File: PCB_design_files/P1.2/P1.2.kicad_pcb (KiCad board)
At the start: 2 copper layers, 127 x 127 mm, 37 parts, among them J1 -EEG_INPUT, J2 +EEG_INPUT, J3 +3.3V, J4 GND, J5 -3V3, J6 EEG_INPUT, J7 STAGE_1_OUT, J8 STAGE_2_OUT, J9 STAGE_3_OUT, U1 INA819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

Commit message: fixed some IC symbols
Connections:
- C6 pad 1: -3V3 -> GND
- C6 pad 2: GND -> -3V3
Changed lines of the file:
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@@
       (stroke (width 0.1) (type solid)) (fill none) (layer "F.Fab"))
     (pad "1" thru_hole rect (at 0 0) (size 1.6 1.6) (drill 0.8) (layers "*.Cu" "*.Mask")
+      (net 1 "GND") (pintype "passive"))
+    (pad "2" thru_hole circle (at 2.5 0) (size 1.6 1.6) (drill 0.8) (layers "*.Cu" "*.Mask")
       (net 8 "-3V3") (pintype "passive"))
-    (pad "2" thru_hole circle (at 2.5 0) (size 1.6 1.6) (drill 0.8) (layers "*.Cu" "*.Mask")
-      (net 1 "GND") (pintype "passive"))
     (model "${KICAD6_3DMODEL_DIR}/Capacitor_THT.3dshapes/CP_Radial_D5.0mm_P2.50mm.wrl"
       (offset (xyz 0 0 0))

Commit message: Created PCB Layout
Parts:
- added J10: BAT+, TestPoint:TestPoint_Loop_D2.50mm_Drill1.0mm, F.Cu at (107.2, 137.6)
- added J11: BOOST, TestPoint:TestPoint_Loop_D2.50mm_Drill1.0mm, F.Cu at (153.9, 106.9)
- J1: value -EEG_INPUT -> EEG_IN-
- J2: value +EEG_INPUT -> EEG_IN+
- R13: value 50k -> 100k
- U4: value TC1044 -> TC1044S
- moved U3 91.5 mm to (146.6, 68.7), turned to 0 degrees
- moved J9 88.2 mm to (181.1, 81.5)
- moved R9 87.4 mm to (154.7, 56.1)
- moved R11 76.8 mm to (168.1, 76.5), turned to 180 degrees
- moved R4 73.7 mm to (130.0, 99.5)
- moved J5 72.7 mm to (142.7, 137.6)
- moved R8 69.6 mm to (150.1, 91.4)
- moved C4 68.0 mm to (146.6, 61.2)
- moved R10 66.0 mm to (154.7, 61.2)
- moved C8 64.8 mm to (158.1, 71.4)
- moved J2 60.8 mm to (81.8, 86.6)
- moved L1 60.7 mm to (119.9, 109.7), turned to -90 degrees
- moved J3 57.7 mm to (119.9, 137.6)
- moved R2 57.6 mm to (98.0, 68.8)
- moved R7 57.4 mm to (130.6, 81.5)
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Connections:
- net Net-(BT1-+) renamed BAT+
- net Net-(J1-Pin_1) renamed /EEG_IN-
- net Net-(J2-Pin_1) renamed /EEG_IN+
- net Net-(J7-Pin_1) renamed STAGE_1_OUT
- C4 pad 1: Net-(J8-Pin_1) -> STAGE_2_OUT
- J8 pad 1: Net-(J8-Pin_1) -> STAGE_2_OUT
- R13 pad 1: Conditioned_EEG -> STAGE_2_OUT
- R13 pad 2: Net-(U3-IN2-) -> Net-(U3-IN1-)
- R8 pad 1: +3.3V -> Net-(U3-IN2-)
- R8 pad 2: Net-(U3-IN1-) -> Conditioned_EEG
- U3 pad 1: Net-(J8-Pin_1) -> STAGE_2_OUT
- U4 pad 1: GND -> Net-(J11-Pin_1)
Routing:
- net +3.3V: track 0.00 -> 172.1 mm
- net -3V3: track 0.00 -> 152.3 mm
- net BAT+: track 0.00 -> 105.3 mm
- net Conditioned_EEG: track 0.00 -> 54.3 mm
- net /EEG_IN-: track 0.00 -> 43.8 mm
- net GND: track 0.00 -> 40.6 mm, vias 0 -> 1
- net /EEG_IN+: track 0.00 -> 39.4 mm
- net Net-(U3-IN1-): track 0.00 -> 34.4 mm
- net Net-(U3-IN2-): track 0.00 -> 34.4 mm
- net STAGE_1_OUT: track 0.00 -> 25.8 mm
- net STAGE_2_OUT: track 0.00 -> 22.7 mm
- net Net-(R2-Pad2): track 0.00 -> 20.8 mm
- net Net-(C8-Pad2): track 0.00 -> 18.1 mm
- net Net-(U4-CAP+): track 0.00 -> 15.7 mm
- net Net-(R2-Pad1): track 0.00 -> 15.0 mm
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- added copper zone on F.Cu, net +3.3V
- added copper zone on B.Cu, net GND
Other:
- board size 127 x 127 mm -> 111.8 x 91.7 mm

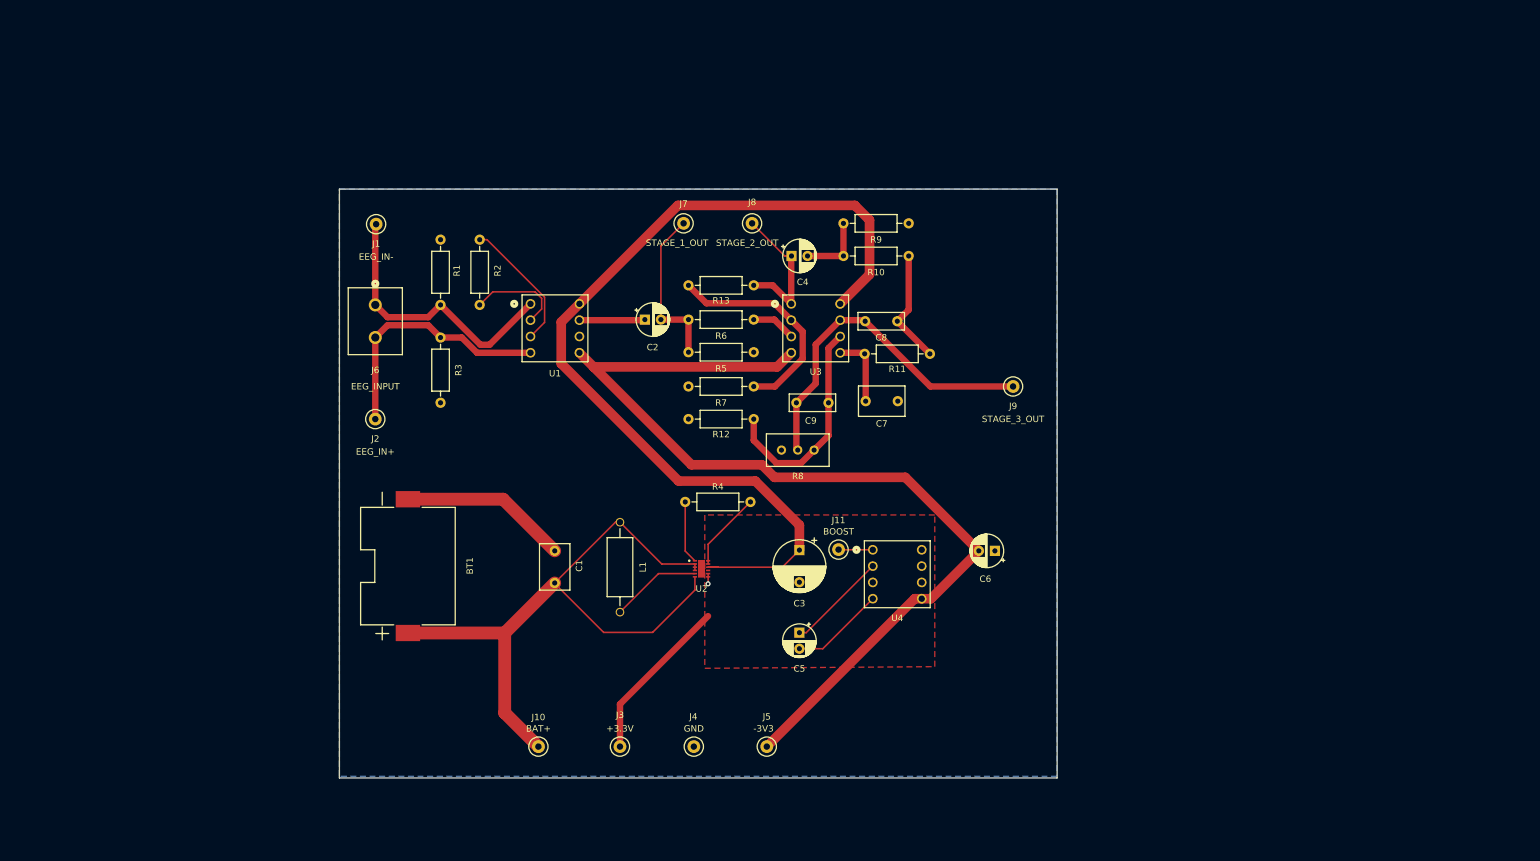
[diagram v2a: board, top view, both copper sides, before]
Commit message: Updated resistor values
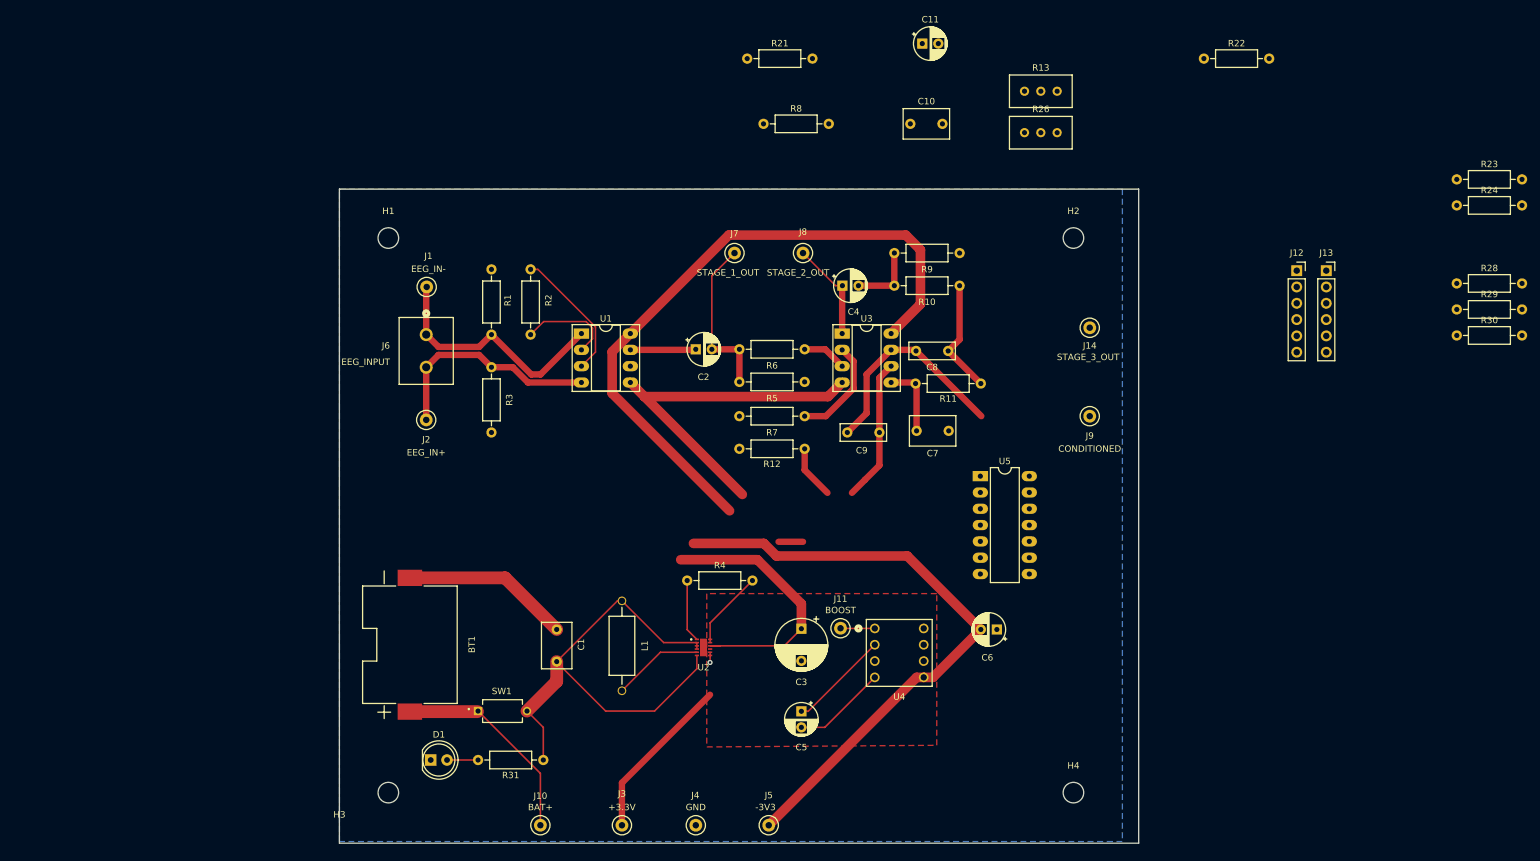
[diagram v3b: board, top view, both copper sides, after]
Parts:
- added C10: 0.1uF, Capacitor_THT:C_Rect_L7.0mm_W4.5mm_P5.00mm, F.Cu at (165.1, 40.6)
- added C11: 10uF, Capacitor_THT:CP_Radial_D5.0mm_P2.50mm, F.Cu at (167.0, 28.1)
- added D1: LED_PWR, LED_THT:LED_D5.0mm, F.Cu at (90.4, 139.7)
- added H1: MountingHole, MountingHole:MountingHole_3.2mm_M3, F.Cu at (83.8, 58.4)
- added H2: MountingHole, MountingHole:MountingHole_3.2mm_M3, F.Cu at (190.5, 58.4)
- added H3: MountingHole, MountingHole:MountingHole_3.2mm_M3, F.Cu at (83.8, 144.8)
- added H4: MountingHole, MountingHole:MountingHole_3.2mm_M3, F.Cu at (190.5, 144.8)
- added J12: Conn_01x06_Pin, Connector_PinSocket_2.54mm:PinSocket_1x06_P2.54mm_Vertical, F.Cu at (225.3, 63.5)
- added J13: Conn_01x06_Pin, Connector_PinSocket_2.54mm:PinSocket_1x06_P2.54mm_Vertical, F.Cu at (229.9, 63.5)
- added J14: STAGE_3_OUT, TestPoint:TestPoint_Loop_D2.50mm_Drill1.0mm, F.Cu at (193.0, 72.4)
- added R21: 100k, Resistor_THT:R_Axial_DIN0207_L6.3mm_D2.5mm_P10.16mm_Horizontal, F.Cu at (139.7, 30.5)
- added R22: 100k, Resistor_THT:R_Axial_DIN0207_L6.3mm_D2.5mm_P10.16mm_Horizontal, F.Cu at (210.8, 30.5)
- added R23: 49.9k, Resistor_THT:R_Axial_DIN0207_L6.3mm_D2.5mm_P10.16mm_Horizontal, F.Cu at (250.2, 49.3)
- added R24: 200k, Resistor_THT:R_Axial_DIN0207_L6.3mm_D2.5mm_P10.16mm_Horizontal, F.Cu at (250.2, 53.3)
- added R26: 100k, Potentiometer_THT:Potentiometer_Bourns_3296W_Vertical, F.Cu at (188.0, 42.0)
- added R28: 10k, Resistor_THT:R_Axial_DIN0207_L6.3mm_D2.5mm_P10.16mm_Horizontal, F.Cu at (250.2, 65.5)
- added R29: 6.98k, Resistor_THT:R_Axial_DIN0207_L6.3mm_D2.5mm_P10.16mm_Horizontal, F.Cu at (250.2, 69.5)
- added R30: 49.9k, Resistor_THT:R_Axial_DIN0207_L6.3mm_D2.5mm_P10.16mm_Horizontal, F.Cu at (250.2, 73.6)
- added R31: 10k, Resistor_THT:R_Axial_DIN0207_L6.3mm_D2.5mm_P10.16mm_Horizontal, F.Cu at (108.0, 139.7)
- added SW1: DS04-254-1S-01BK, DS04_254_1S_01BK:SW_DS04-254-1S-01BK, F.Cu at (101.6, 132.1)
- added U5: LTC1059CS#PBF, Package_DIP:DIP-14_W7.62mm_LongPads, F.Cu at (176.0, 95.5)
- J9: value STAGE_3_OUT -> CONDITIONED
- R10: value 600 -> 604
- R12: value 2.5k -> 2.49k
- R13: footprint Resistor_THT:R_Axial_DIN0207_L6.3mm_D2.5mm_P10.16mm_Horizontal -> Potentiometer_THT:Potentiometer_Bourns_3296W_Vertical
- R2: value 8.5k -> 8.2k
- R8: value 100k -> 49.9k; footprint Potentiometer_THT:Potentiometer_Bourns_3296W_Vertical -> Resistor_THT:R_Axial_DIN0207_L6.3mm_D2.5mm_P10.16mm_Horizontal
- U1, U3: footprint 1-2199298-2:CONN8_1-2199298-2_TEC -> Package_DIP:DIP-8_W7.62mm_Socket_LongPads
- moved R13 56.1 mm to (188.0, 35.6), turned to 0 degrees
- moved R8 51.4 mm to (142.2, 40.6)
- moved J9 12.8 mm to (193.0, 86.2)
- moved J1 12.6 mm to (89.8, 66.0)
- moved J10 12.2 mm to (107.5, 149.9)
- moved J3 12.2 mm to (120.2, 149.9)
- moved J4 12.2 mm to (131.7, 149.9)
- moved J5 12.2 mm to (143.1, 149.9)
- moved BT1 12.2 mm to (87.2, 121.8)
- moved C1 12.2 mm to (110.0, 124.4)
- moved C3 12.2 mm to (148.1, 119.3)
- moved C5 12.2 mm to (148.1, 132.1)
- moved C6 12.2 mm to (178.6, 119.4)
- moved J11 12.2 mm to (154.2, 119.2)
- moved R4 12.2 mm to (130.4, 111.8)
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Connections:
- C1 pad 1: BAT+ -> Net-(U2-EN)
- C8 pad 1: Conditioned_EEG -> Net-(C10-Pad1)
- C9 pad 1: Conditioned_EEG -> Net-(C10-Pad1)
- L1 pad 1: BAT+ -> Net-(U2-EN)
- R13 pad 1: STAGE_2_OUT -> Net-(U3-IN1-)
- R13 pad 2: Net-(U3-IN1-) -> STAGE_2_OUT
- R8 pad 2: Conditioned_EEG -> Net-(C10-Pad1)
- U2 pad 2: BAT+ -> Net-(U2-EN)
- U2 pad 3: BAT+ -> Net-(U2-EN)
- U2 pad 4: BAT+ -> Net-(U2-EN)
- U2 pad 6: BAT+ -> Net-(U2-EN)
- U3 pad 7: Conditioned_EEG -> Net-(U3-OUT2)
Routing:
- net Net-(U2-EN): track 0.00 -> 77.6 mm
- net BAT+: track 105.3 -> 32.4 mm
- net Conditioned_EEG: track 54.3 -> 34.0 mm
- net Net-(U3-IN1-): track 34.4 -> 16.2 mm
- net STAGE_2_OUT: track 22.7 -> 15.7 mm
- net /EEG_IN-: track 43.8 -> 38.8 mm
- net Net-(D1-A): track 0.00 -> 4.83 mm
- net /EEG_IN+: track 39.4 -> 34.9 mm
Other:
- board size 111.8 x 91.7 mm -> 124.5 x 101.9 mm

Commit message: Redesigning PCB
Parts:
- moved R12 86.9 mm to (233.7, 109.2)
- moved R5 86.9 mm to (223.5, 98.8)
- moved R6 86.9 mm to (223.5, 93.7)
- moved R7 86.9 mm to (223.5, 104.1)
- moved J13 75.0 mm to (243.8, 137.2), turned to 90 degrees
- moved C6 65.1 mm to (114.3, 109.2), turned to 90 degrees
- moved J12 59.5 mm to (256.5, 114.2), turned to -90 degrees
- moved C9 55.7 mm to (210.9, 91.4)
- moved C7 52.8 mm to (223.6, 83.6)
- moved C8 52.8 mm to (218.5, 71.1)
- moved R11 52.8 mm to (228.6, 76.2)
- moved R10 51.0 mm to (213.4, 61.0)
- moved R9 51.0 mm to (213.4, 55.9)
- moved J7 31.2 mm to (116.3, 38.1)
- moved J8 31.2 mm to (127.0, 38.1)
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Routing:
- net +3.3V: track 172.1 -> 41.1 mm
- net -3V3: track 152.3 -> 53.3 mm
- net Net-(U3-IN2-): track 34.4 -> 0.00 mm
- net Conditioned_EEG: track 34.0 -> 0.00 mm
- net Net-(U2-EN): track 77.6 -> 45.6 mm
- net STAGE_1_OUT: track 25.8 -> 0.00 mm
- net GND: track 40.6 -> 19.8 mm
- net Net-(C8-Pad2): track 18.1 -> 0.00 mm
- net Net-(U3-IN1-): track 16.2 -> 0.00 mm
- net STAGE_2_OUT: track 15.7 -> 0.00 mm
- net Net-(U3-IN2+): track 11.3 -> 0.00 mm
- net Net-(C4-Pad2): track 10.7 -> 0.00 mm
- net Net-(U1-OUT): track 10.2 -> 0.00 mm
- net Net-(U3-IN1+): track 6.93 -> 0.00 mm
- net Net-(U4-CAP-): track 14.7 -> 7.89 mm
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- removed copper zone on F.Cu, net +3.3V

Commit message: Updated PCB layout
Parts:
- moved R5 97.9 mm to (128.3, 76.2), turned to -90 degrees
- moved C7 92.1 mm to (135.2, 109.2), turned to 0 degrees
- moved R6 91.9 mm to (133.3, 76.2), turned to -90 degrees
- moved R7 89.3 mm to (138.7, 76.2), turned to -90 degrees
- moved R12 84.7 mm to (149.1, 104.1), turned to -90 degrees
- moved J13 84.3 mm to (159.6, 133.3), turned to 0 degrees
- moved J12 80.5 mm to (182.6, 146.1), turned to 180 degrees
- moved R23 76.3 mm to (175.3, 63.5), turned to -90 degrees
- moved R24 72.7 mm to (180.3, 73.7), turned to 90 degrees
- moved R28 71.3 mm to (182.9, 88.9), turned to 90 degrees
- moved R21 70.4 mm to (170.2, 94.0), turned to -90 degrees
- moved R30 69.5 mm to (190.5, 109.2), turned to -90 degrees
- moved R29 67.5 mm to (195.6, 109.2), turned to -90 degrees
- moved R22 67.1 mm to (177.8, 88.9), turned to 90 degrees
- moved C11 66.3 mm to (175.1, 94.0)
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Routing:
- net +3.3V: track 41.1 -> 290.4 mm
- net -3V3: track 53.3 -> 138.6 mm, vias 0 -> 1
- net CLK: track 0.00 -> 79.4 mm
- net Conditioned_EEG: track 0.00 -> 66.1 mm
- net STAGE_3_OUT: track 0.00 -> 63.7 mm
- net STAGE_2_OUT: track 0.00 -> 44.8 mm
- net Net-(C10-Pad1): track 0.00 -> 40.6 mm
- net Net-(U3-IN2+): track 0.00 -> 38.3 mm
- net STAGE_1_OUT: track 0.00 -> 29.8 mm
- net Net-(U2-EN): track 45.6 -> 73.6 mm
- net Net-(U3-IN1-): track 0.00 -> 21.1 mm
- net Net-(U3-OUT2): track 0.00 -> 18.5 mm
- net Net-(C8-Pad2): track 0.00 -> 17.3 mm
- net Net-(U3-IN2-): track 0.00 -> 17.2 mm
- net Net-(C4-Pad2): track 0.00 -> 15.9 mm
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
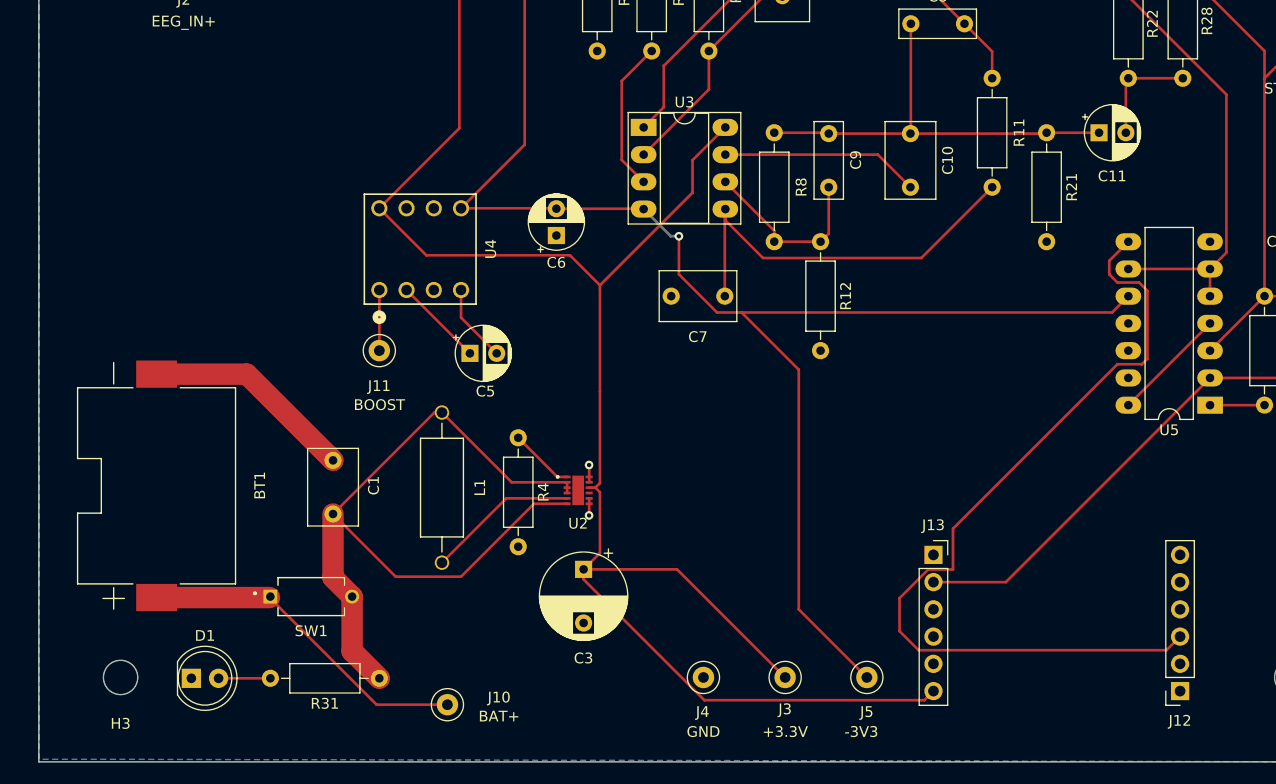
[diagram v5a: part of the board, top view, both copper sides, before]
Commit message: Design review changes
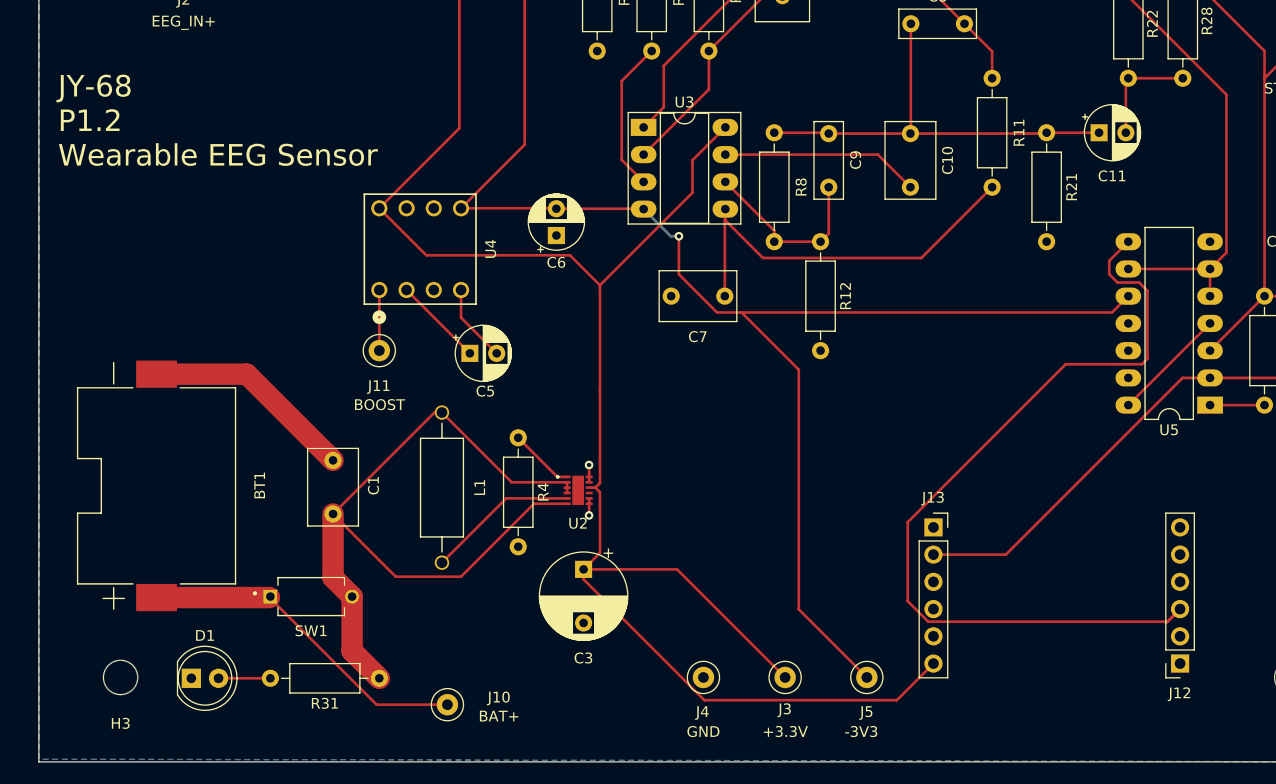
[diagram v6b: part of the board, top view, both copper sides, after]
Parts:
- moved J12 2.56 mm to (182.6, 143.5)
- moved J13 2.56 mm to (159.6, 130.8)
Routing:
- net +3.3V: track 290.4 -> 291.5 mm
- net Conditioned_EEG: track 66.1 -> 65.1 mm
- net CLK: track 79.4 -> 78.8 mm
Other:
- board text added: "JY-68 P1.2 Wearable EEG Sensor"
- board text added: "JY-68: Albert Chris Connor Peak T"
